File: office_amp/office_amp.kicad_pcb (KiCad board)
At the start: 4 copper layers, 120 x 100 mm, 105 parts, among them J1 Jack-DC, J2 Conn_01x03_Female, J3 Conn_01x02_Female, J4 Conn_01x02_Female, J5 Conn_01x02_Female, J6 Conn_01x02_Female, J7 Screw_Terminal_01x04, J8 Conn_01x03_Female, K1 EC2-24NU, K2 EC2-24NU, K3 EC2-24NU, K4 EC2-24NU, Q1 DMT6012LSS, Q2 BC858, Q3 BC858, Q4 BC850, Q5 BC850, U1 LM74700, U10 DS1882E, U12 TL082, U2 TBA_2-2421, U3 TL082, U4 TBA_2-2421, U5 MH-M18, U6 TPA3123D2, U7 TL082, U8 IL300, U9 IL300

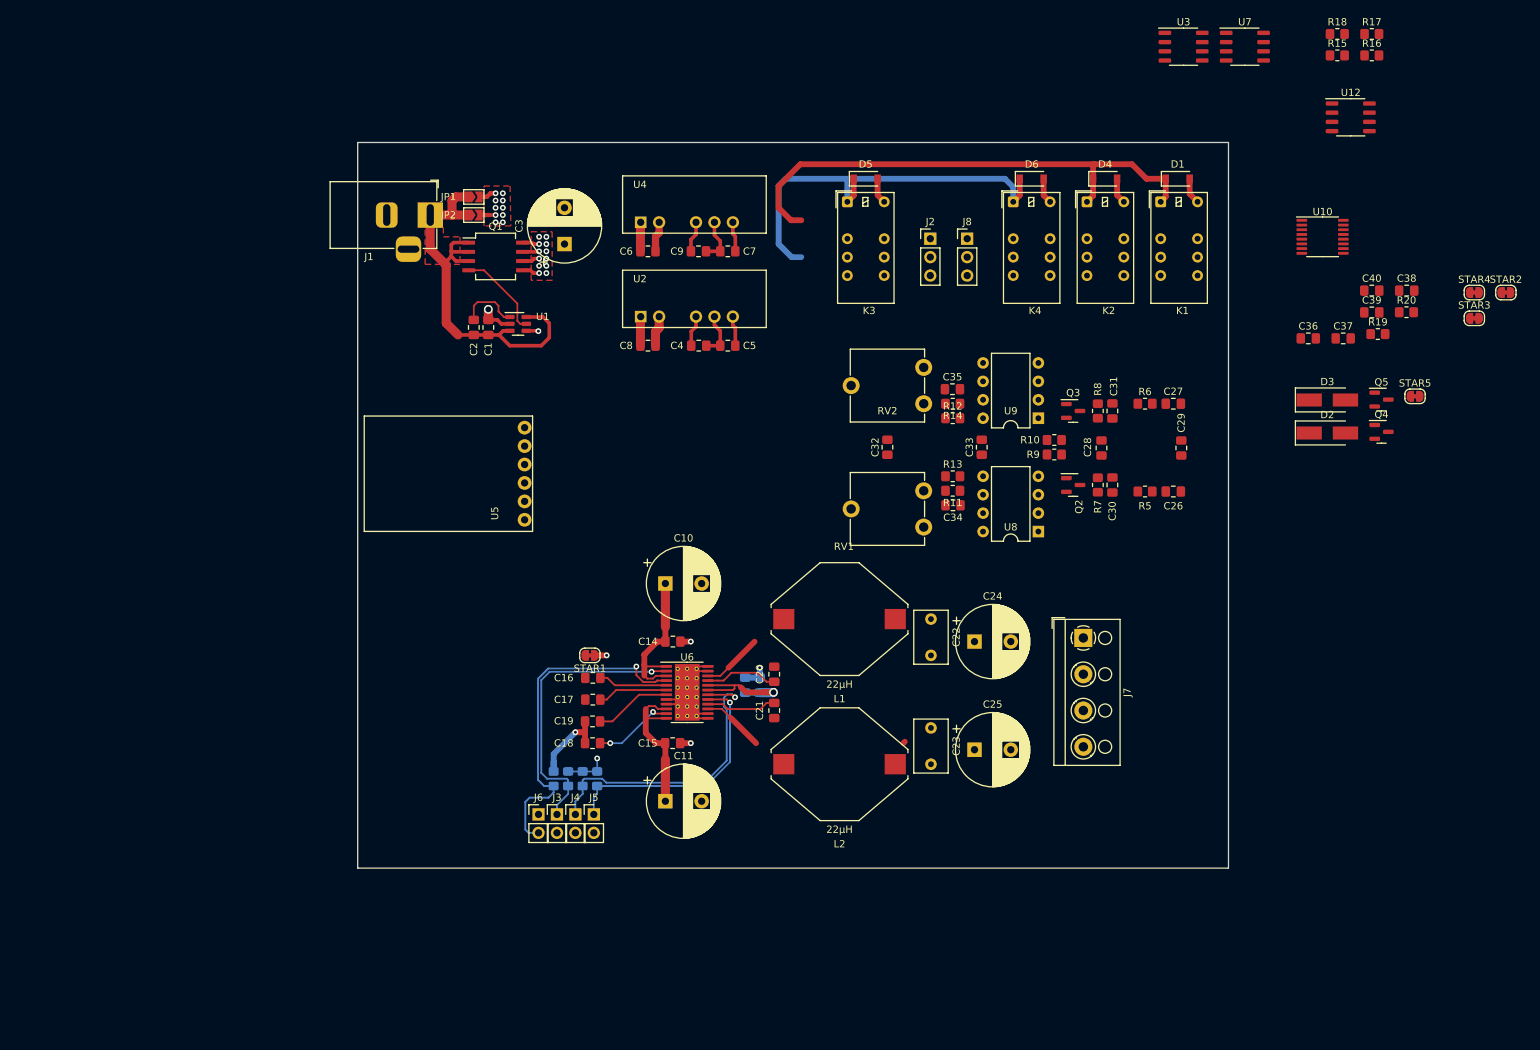
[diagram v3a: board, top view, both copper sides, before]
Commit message: First positioning of new components (top site), added mounting holes for case  compabillity (Donau 523178)
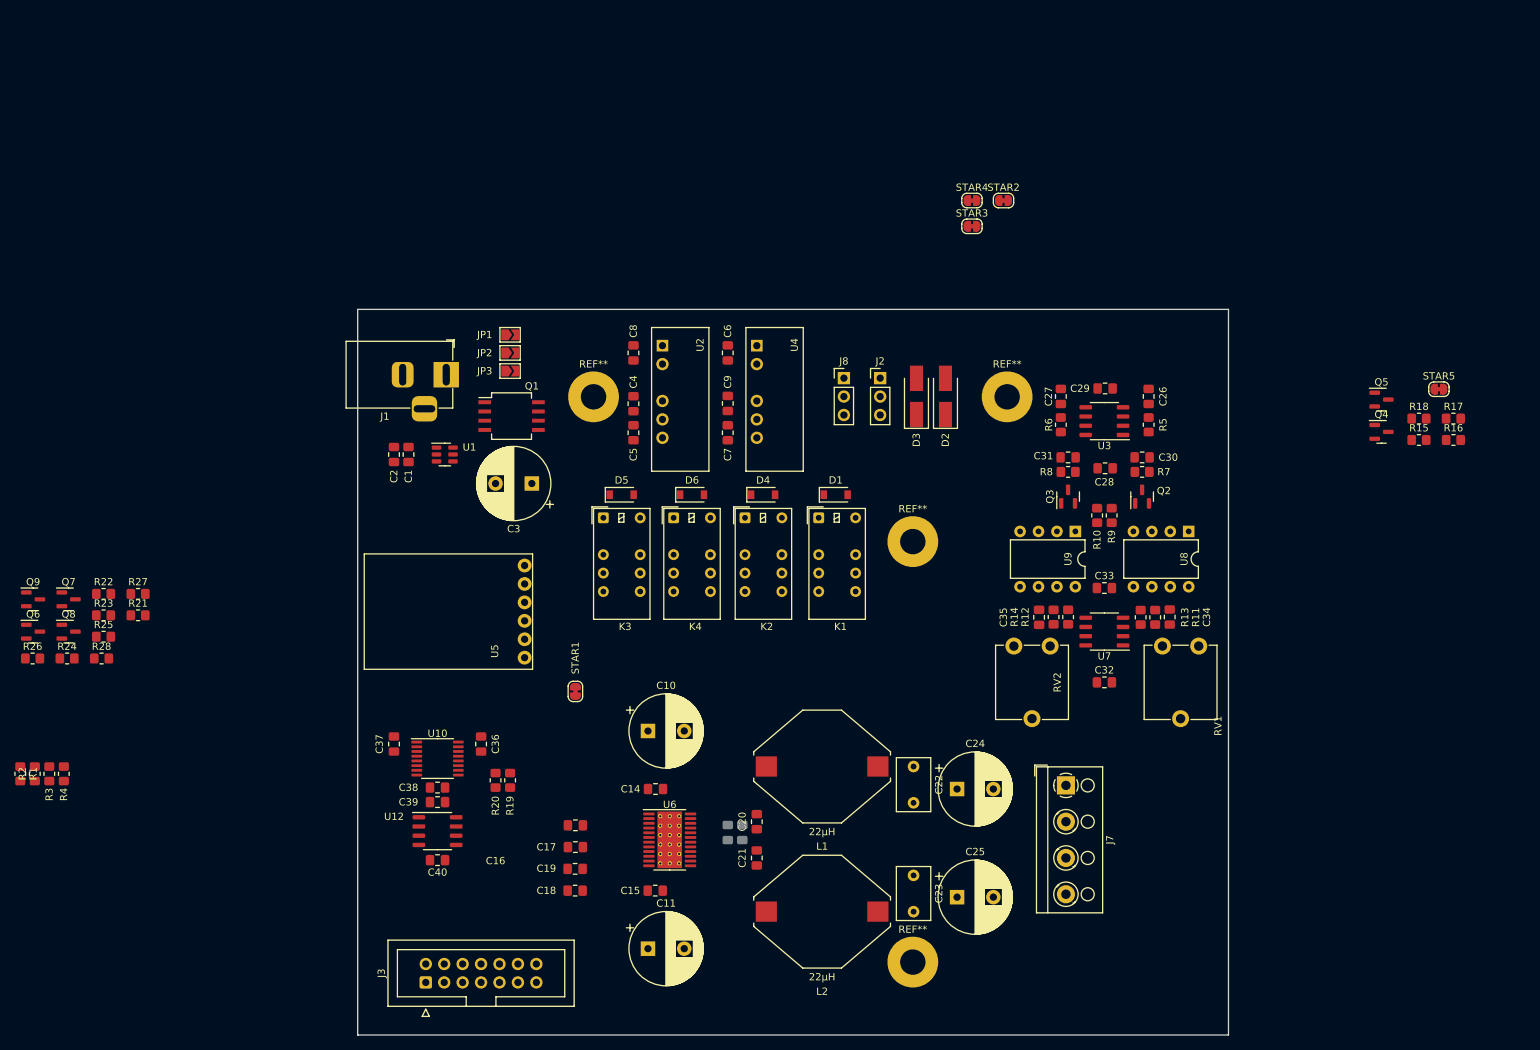
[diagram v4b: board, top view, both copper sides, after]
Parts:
- removed J4, J5, J6: Conn_01x02_Female, Connector_PinHeader_2.54mm:PinHeader_1x02_P2.54mm_Vertical
- added JP3: Jumper_2_Open, Jumper:SolderJumper-2_P1.3mm_Open_TrianglePad1.0x1.5mm, F.Cu at (111.0, 66.5)
- added Q6: BC856, Package_TO_SOT_SMD:SOT-23, F.Cu at (45.3, 102.4)
- added Q7: BC850, Package_TO_SOT_SMD:SOT-23, F.Cu at (50.2, 98.0)
- added Q8: BC856, Package_TO_SOT_SMD:SOT-23, F.Cu at (50.2, 102.4)
- added Q9: BC856, Package_TO_SOT_SMD:SOT-23, F.Cu at (45.3, 98.0)
- added R21: 10k, Resistor_SMD:R_0805_2012Metric_Pad1.20x1.40mm_HandSolder, F.Cu at (59.7, 100.2)
- added R22: 10k, Resistor_SMD:R_0805_2012Metric_Pad1.20x1.40mm_HandSolder, F.Cu at (55.0, 97.2)
- added R23: 10k, Resistor_SMD:R_0805_2012Metric_Pad1.20x1.40mm_HandSolder, F.Cu at (55.0, 100.2)
- added R24: 10k, Resistor_SMD:R_0805_2012Metric_Pad1.20x1.40mm_HandSolder, F.Cu at (50.0, 106.1)
- added R25: 10k, Resistor_SMD:R_0805_2012Metric_Pad1.20x1.40mm_HandSolder, F.Cu at (55.0, 103.1)
- added R26: 10k, Resistor_SMD:R_0805_2012Metric_Pad1.20x1.40mm_HandSolder, F.Cu at (45.2, 106.1)
- added R27: 10k, Resistor_SMD:R_0805_2012Metric_Pad1.20x1.40mm_HandSolder, F.Cu at (59.7, 97.2)
- added R28: 10k, Resistor_SMD:R_0805_2012Metric_Pad1.20x1.40mm_HandSolder, F.Cu at (54.7, 106.1)
- added REF**: MountingHole_3.5mm_Pad, MountingHole:MountingHole_3.5mm_Pad, F.Cu at (179.5, 70.0)
- added REF**: MountingHole_3.5mm_Pad, MountingHole:MountingHole_3.5mm_Pad, F.Cu at (166.5, 147.9)
- added REF**: MountingHole_3.5mm_Pad, MountingHole:MountingHole_3.5mm_Pad, F.Cu at (166.5, 90.0)
- added REF**: MountingHole_3.5mm_Pad, MountingHole:MountingHole_3.5mm_Pad, F.Cu at (122.5, 70.0)
- J3: value Conn_01x02_Female -> Conn_02x07_Odd_Even; footprint Connector_PinHeader_2.54mm:PinHeader_1x02_P2.54mm_Vertical -> Connector_IDC:IDC-Header_2x07_P2.54mm_Vertical
- R1, R2, R3, R4: moved to F.Cu
- R15, R16, R17, R18: value R -> 10k
- moved U12 159.7 mm to (101.0, 129.9)
- moved C40 150.8 mm to (101.0, 133.9), turned to 180 degrees
- moved C38 150.1 mm to (101.0, 123.9), turned to 180 degrees
- moved C39 145.4 mm to (101.0, 125.9), turned to 180 degrees
- moved C37 142.3 mm to (95.0, 117.9), turned to -90 degrees
- moved U10 141.6 mm to (101.0, 119.9)
- moved R20 141.1 mm to (109.0, 122.9), turned to 90 degrees
- moved R19 134.5 mm to (111.0, 122.9), turned to 90 degrees
- moved C36 127.0 mm to (107.0, 117.9), turned to 90 degrees
- moved U7 82.9 mm to (192.9, 102.4), turned to 180 degrees
- moved R1 79.5 mm to (43.5, 122.0)
- moved R2 75.5 mm to (45.5, 122.0)
- moved R3 71.5 mm to (47.5, 122.0)
- moved STAR2 70.4 mm to (179.0, 43.0)
- moved STAR3 70.4 mm to (174.7, 46.5)
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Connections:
- C17 pad 2: Net-(U12-Pad2) -> Net-(C17-Pad2)
- C40 pad 2: GNDA -> -5V
- J3 pad 1: /Class_D/~{SD} -> +5V
- J3 pad 2: GNDREF -> GNDD
- R1 pad 1: V+ -> /Class_D/GAIN1
- R1 pad 2: /Class_D/GAIN1 -> GNDREF
- R2 pad 1: V+ -> /Class_D/GAIN0
- R2 pad 2: /Class_D/GAIN0 -> GNDREF
- R3 pad 1: V+ -> /Class_D/~{SD}
- R3 pad 2: /Class_D/~{SD} -> GNDREF
- R4 pad 1: /Class_D/MUTE -> +3V3
- R4 pad 2: GNDREF -> /Class_D/MUTE
- U12 pad 1: unconnected-(U12-Pad1) -> Net-(C17-Pad2)
- U12 pad 2: Net-(U12-Pad2) -> Net-(C17-Pad2)
- U12 pad 4: GNDA -> -5V
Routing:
- net GNDREF: track 504.6 -> 0.00 mm, vias 6 -> 0
- net V+: track 425.4 -> 0.00 mm, vias 25 -> 0
- net GND_Input: track 67.1 -> 0.00 mm
- net +5VA: track 63.1 -> 0.00 mm
- net /Power/Vin: track 59.6 -> 0.00 mm
- net /Class_D/MUTE: track 47.7 -> 0.00 mm, vias 1 -> 0
- net /Class_D/GAIN0: track 41.1 -> 0.00 mm, vias 1 -> 0
- net /Class_D/~{SD}: track 40.0 -> 0.00 mm, vias 1 -> 0
- net /Class_D/GAIN1: track 35.2 -> 0.00 mm, vias 1 -> 0
- net Net-(Q1-PadG): track 12.4 -> 0.00 mm
- net /Class_D/VCLAMP: track 11.0 -> 0.00 mm, vias 2 -> 0
- net /Class_D/BYPASS: track 10.7 -> 0.00 mm
- net /Class_D/BSL: track 10.1 -> 0.00 mm
- net /Class_D/BSR: track 9.76 -> 0.00 mm
- net /Class_D/RIN: track 9.65 -> 0.00 mm
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- removed copper zone on F.Cu, net /Power/Vin
- removed copper zone on F.Cu, net V+

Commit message: Placement first try
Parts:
- Q4, Q5, Q6, Q7, Q8, Q9, R1, R15, R16, R17, R18, R2, R21, R22, R23, R24, R25, R26, R27, R28, R3, R4, STAR2, STAR3, STAR4, STAR5: moved to B.Cu
- moved STAR5 120.5 mm to (121.0, 93.5), turned to 90 degrees
- moved R17 110.4 mm to (135.0, 104.0), turned to 180 degrees
- moved R18 108.4 mm to (133.0, 106.0)
- moved Q5 105.3 mm to (131.0, 103.0), turned to 90 degrees
- moved R16 93.0 mm to (153.0, 106.0)
- moved R15 85.9 mm to (155.0, 104.0), turned to 180 degrees
- moved Q4 84.9 mm to (151.0, 103.0), turned to 90 degrees
- moved Q9 81.9 mm to (115.0, 141.0), turned to 90 degrees
- moved R26 81.6 mm to (118.0, 143.0), turned to -90 degrees
- moved Q6 74.1 mm to (108.5, 141.0), turned to 90 degrees
- moved R1 71.9 mm to (114.0, 136.0), turned to 180 degrees
- moved R28 71.2 mm to (115.0, 144.0), turned to 180 degrees
- moved R23 69.2 mm to (108.5, 144.0), turned to 180 degrees
- moved R21 67.2 mm to (111.5, 143.0), turned to -90 degrees
- moved Q8 64.6 mm to (102.0, 141.0), turned to 90 degrees
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
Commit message: Completed PCB-Layout V1
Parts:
- moved D1 17.5 mm to (156.7, 101.0), turned to 180 degrees
- moved D4 17.5 mm to (146.5, 101.0), turned to 180 degrees
- moved D6 17.5 mm to (136.5, 101.0), turned to 180 degrees
- moved D5 17.5 mm to (126.5, 101.0), turned to 180 degrees
- moved K2 12.6 mm to (149.0, 98.0), turned to 180 degrees
- moved K1 12.5 mm to (159.0, 98.0), turned to 180 degrees
- moved K4 12.5 mm to (139.0, 98.0), turned to 180 degrees
- moved STAR5 12.5 mm to (121.0, 106.0), turned to 180 degrees
- moved K3 12.4 mm to (129.0, 98.0), turned to 180 degrees
- moved STAR2 6.00 mm to (137.0, 80.0)
- moved STAR4 6.00 mm to (137.0, 74.0)
- moved C35 3.13 mm to (187.0, 100.0)
- moved R11 3.13 mm to (203.0, 100.0), turned to 90 degrees
- moved R12 2.93 mm to (185.0, 100.0)
- moved R14 2.93 mm to (183.0, 100.0)
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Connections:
- J3 pad 10: SCL -> SDA
- J3 pad 12: SDA -> SCL
- J8 pad 1: GND_BT -> GND_USB
- K2 pad 3: GND_BT -> GND_USB
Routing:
- net GNDREF: track 0.00 -> 372.5 mm, vias 0 -> 10
- net V+: track 0.00 -> 368.7 mm, vias 0 -> 11
- net +5V: track 0.00 -> 329.5 mm, vias 0 -> 7
- net GNDA: track 0.00 -> 284.1 mm, vias 0 -> 10
- net -5V: track 0.00 -> 223.3 mm, vias 0 -> 7
- net GNDD: track 0.00 -> 181.9 mm, vias 0 -> 6
- net GND_Input: track 0.00 -> 135.5 mm, vias 0 -> 3
- net +3V3: track 0.00 -> 116.3 mm, vias 0 -> 7
- net +5VA: track 0.00 -> 96.9 mm, vias 0 -> 2
- net SELECT-Analog: track 0.00 -> 93.8 mm, vias 0 -> 1
- net SELECT-BT: track 0.00 -> 77.2 mm, vias 0 -> 1
- net BT-KEY: track 0.00 -> 72.6 mm
- net L-In: track 0.00 -> 71.0 mm, vias 0 -> 3
- net -5VA: track 0.00 -> 68.2 mm, vias 0 -> 1
- net R-In-ISO: track 0.00 -> 66.9 mm, vias 0 -> 2
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- added copper zone on F.Cu, net /Power/Vin
- added copper zone on B.Cu, net GNDA
- added copper zone on F.Cu, net GNDA
- added copper zone on In1.Cu, net GNDA
- added copper zone on B.Cu, net GNDREF
- added copper zone on F.Cu, net GNDREF
- added copper zone on In1.Cu, net GNDREF
- added copper zone on B.Cu, net GND_Input
- added copper zone on F.Cu, net GND_Input
- added copper zone on In1.Cu, net GND_Input
- added copper zone on F.Cu, net V+
- added copper zone on In2.Cu, net V+
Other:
- board text added: "Analog-IN ext. Analog-IN int."
- board text added: "C@mpuswoche"
- board text added: "CW-AMP V1.0 Lars Nienhaus"
- board text added: "L+"
- board text added: "L-"
- board text added: "R+"
- board text added: "R-"
- board text added: "Westfälische Hochschule"

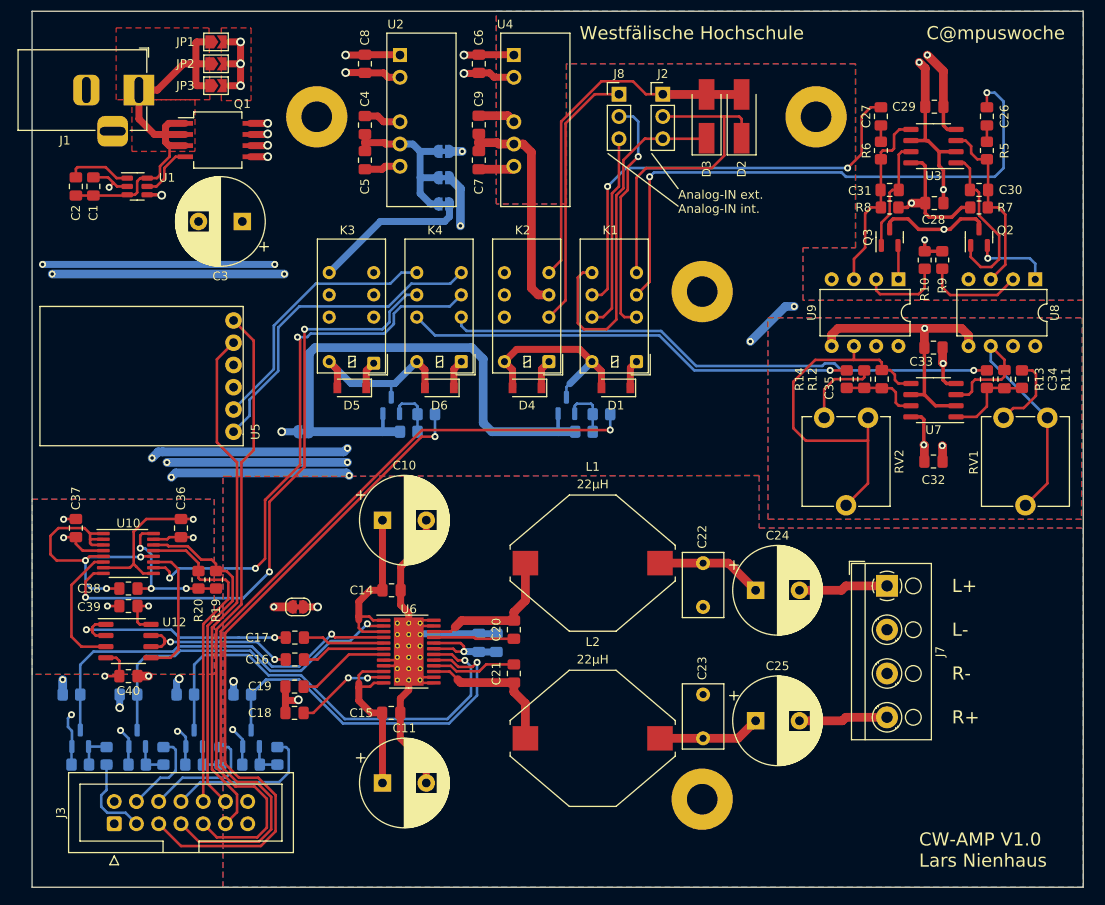
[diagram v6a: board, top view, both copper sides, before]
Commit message: added testpoints, corrected footprints, removed ground loop dgnd gnda
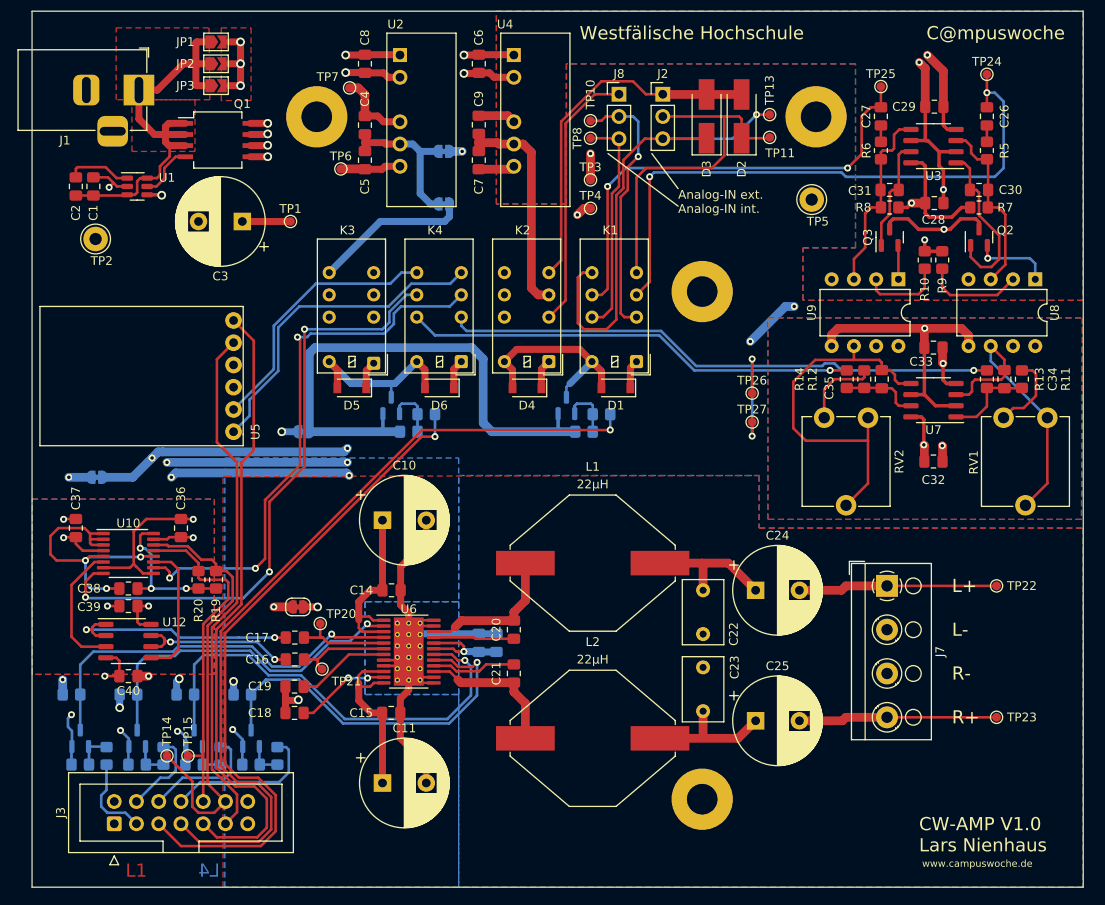
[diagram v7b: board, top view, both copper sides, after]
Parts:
- added TP1: TestPoint, TestPoint:TestPoint_Pad_D1.0mm, F.Cu at (119.5, 82.0)
- added TP10: TestPoint, TestPoint:TestPoint_Pad_D1.0mm, F.Cu at (153.8, 70.5)
- added TP11: TestPoint, TestPoint:TestPoint_Pad_D1.0mm, F.Cu at (174.2, 72.4)
- added TP13: TestPoint, TestPoint:TestPoint_Pad_D1.0mm, F.Cu at (174.2, 69.8)
- added TP14: TestPoint, TestPoint:TestPoint_Pad_D1.0mm, F.Cu at (105.4, 143.0)
- added TP15: TestPoint, TestPoint:TestPoint_Pad_D1.0mm, F.Cu at (107.8, 143.0)
- added TP2: TestPoint, TestPoint:TestPoint_Loop_D2.60mm_Drill1.4mm_Beaded, F.Cu at (97.2, 84.0)
- added TP20: TestPoint, TestPoint:TestPoint_Pad_D1.0mm, F.Cu at (122.9, 127.9)
- added TP21: TestPoint, TestPoint:TestPoint_Pad_D1.0mm, F.Cu at (123.1, 133.1)
- added TP22: TestPoint, TestPoint:TestPoint_Pad_D1.0mm, F.Cu at (200.1, 123.6)
- added TP23: TestPoint, TestPoint:TestPoint_Pad_D1.0mm, F.Cu at (200.1, 138.6)
- added TP24: TestPoint, TestPoint:TestPoint_Pad_D1.0mm, F.Cu at (199.0, 65.2)
- added TP25: TestPoint, TestPoint:TestPoint_Pad_D1.0mm, F.Cu at (186.9, 66.6)
- added TP26: TestPoint, TestPoint:TestPoint_Pad_D1.0mm, F.Cu at (172.2, 101.6)
- added TP27: TestPoint, TestPoint:TestPoint_Pad_D1.0mm, F.Cu at (172.2, 104.9)
- added TP3: TestPoint, TestPoint:TestPoint_Pad_D1.0mm, F.Cu at (153.8, 77.2)
- added TP4: TestPoint, TestPoint:TestPoint_Pad_D1.0mm, F.Cu at (153.8, 80.5)
- added TP5: TestPoint, TestPoint:TestPoint_Loop_D2.60mm_Drill1.4mm_Beaded, F.Cu at (179.0, 79.5)
- added TP6: TestPoint, TestPoint:TestPoint_Pad_D1.0mm, F.Cu at (125.2, 76.0)
- added TP7: TestPoint, TestPoint:TestPoint_Pad_D1.0mm, F.Cu at (126.2, 66.8)
- added TP8: TestPoint, TestPoint:TestPoint_Pad_D1.0mm, F.Cu at (153.8, 72.5)
- moved STAR3 52.3 mm to (97.4, 111.2), turned to 0 degrees
- moved C22 3.10 mm to (166.6, 124.1)
- moved C23 3.10 mm to (166.6, 132.9)
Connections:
- STAR3 pad 2: Net-(C4-Pad1) -> GNDA
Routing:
- net GNDD: track 181.9 -> 106.4 mm, vias 6 -> 4
- net +5V: track 329.5 -> 262.6 mm, vias 7 -> 5
- net -5VA: track 68.2 -> 89.4 mm, vias 1 -> 2
- net GND_Input: track 135.5 -> 154.3 mm
- net L-In-An: track 41.3 -> 54.6 mm, vias 0 -> 1
- net /Class_D/R-Out: track 10.2 -> 22.7 mm
- net /Class_D/L-Out: track 10.2 -> 22.7 mm
- net SCL: track 38.7 -> 50.3 mm
- net +5VA: track 96.9 -> 106.7 mm, vias 2 -> 3
- net L-In-OPA: track 51.6 -> 60.7 mm, vias 1 -> 2
- net GNDA: track 284.1 -> 290.7 mm
- net V+: track 368.7 -> 374.2 mm
- net R-In-OPA: track 63.3 -> 68.0 mm, vias 1 -> 2
- net -5V: track 223.3 -> 227.8 mm
- net R-In-USB: track 27.1 -> 30.6 mm
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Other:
- board text added: "42Volt.de"
- board text added: "L1"
- board text added: "L2"
- board text added: "L3"
- board text added: "L4"
- board text added: "www.campuswoche.de"
